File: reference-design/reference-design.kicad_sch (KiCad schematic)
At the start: 21 parts

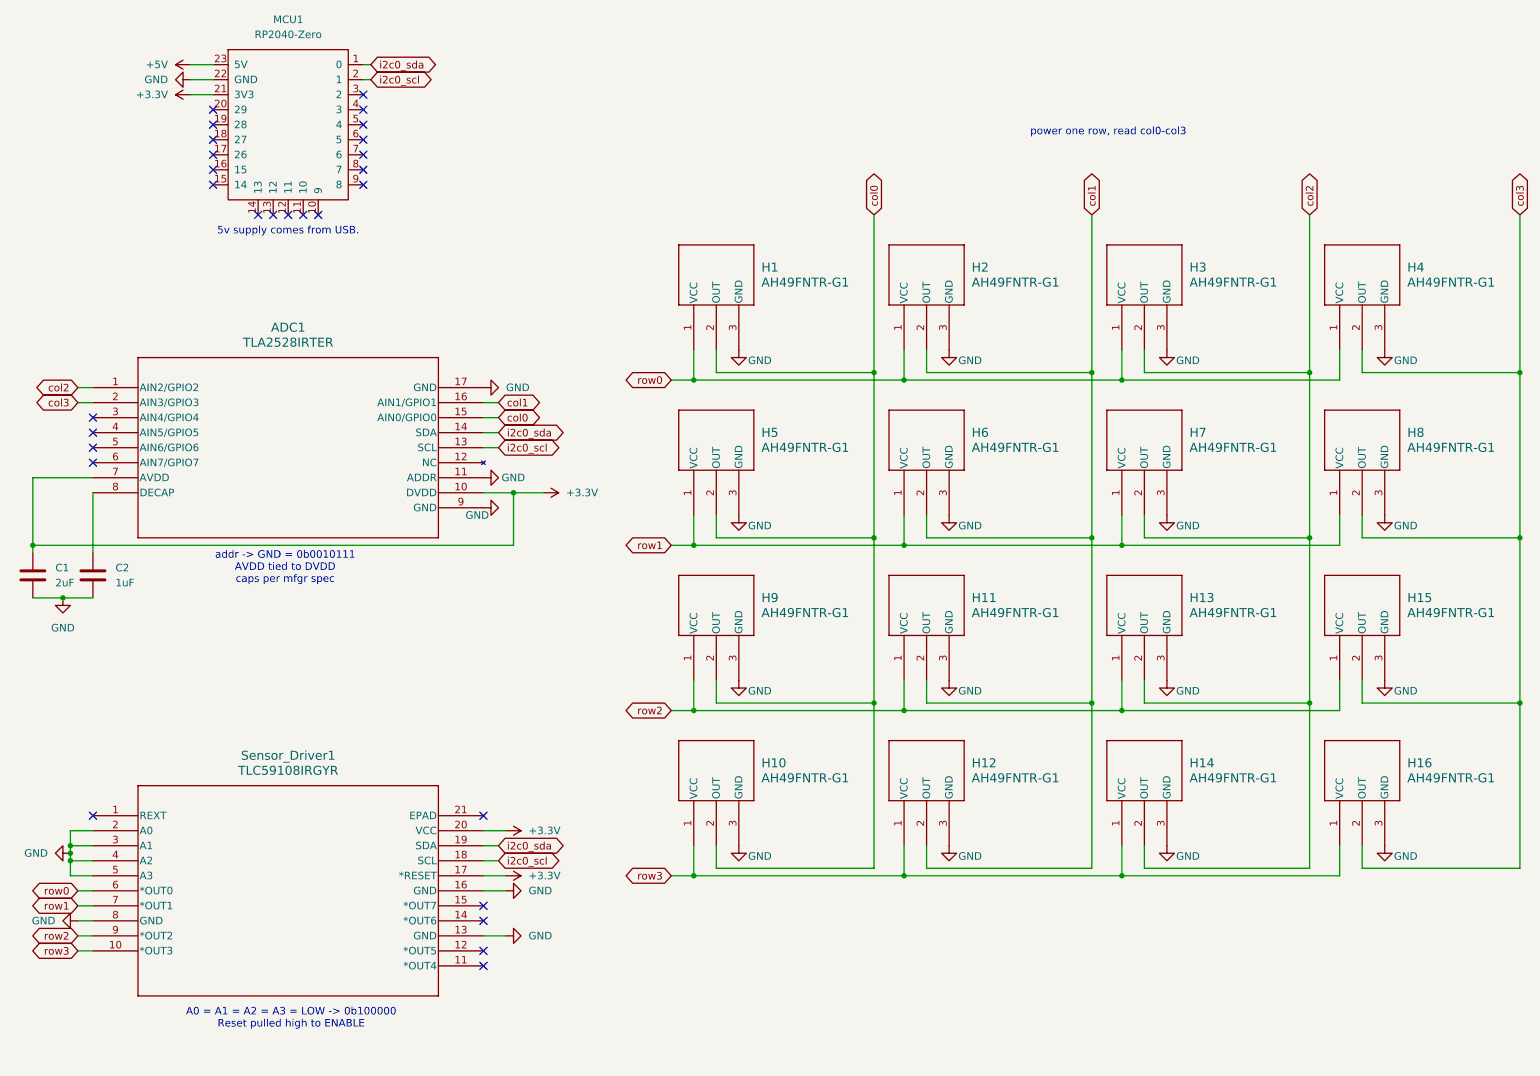
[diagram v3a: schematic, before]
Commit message: fix all but 7 warnings in ERC and DRC. notably, REXT issue still needs to be resolved
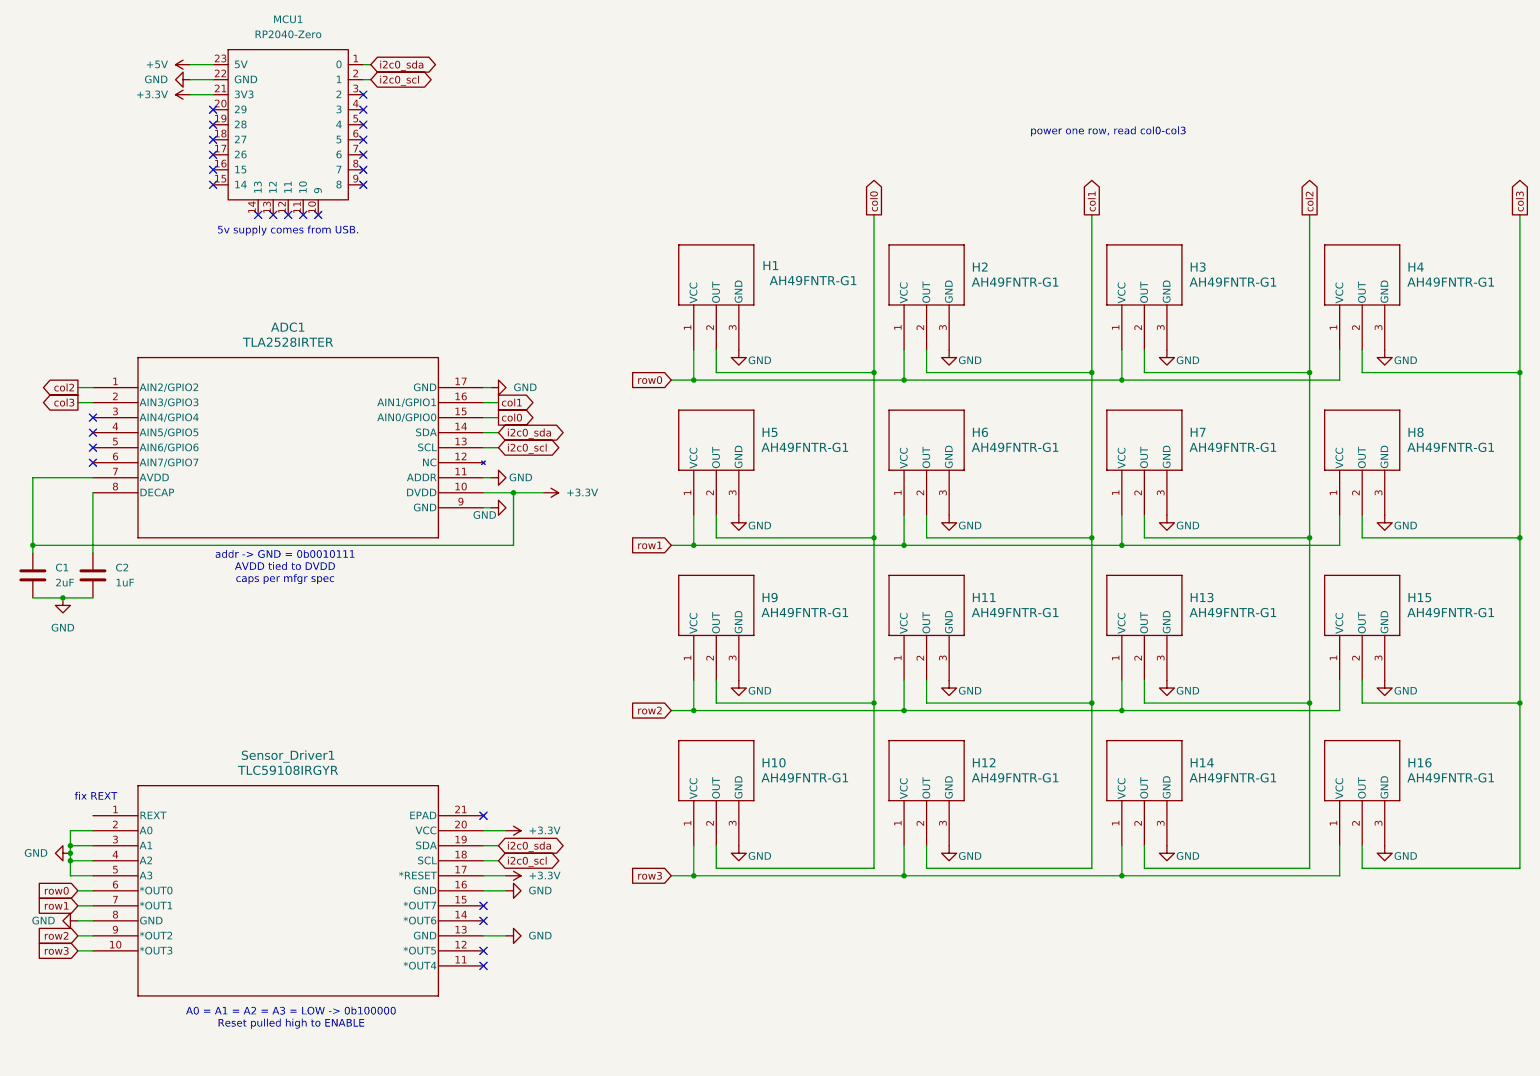
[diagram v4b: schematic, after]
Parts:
- ADC1: symbol TLA2528IRTER:TLA2528IRTER -> TLA2528IRTER_mod:TLA2528IRTER
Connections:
- no-connect marks 28 -> 27
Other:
- note added: "fix REXT"
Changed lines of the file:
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@@
 	(title_block
 		(title "ParaKeyt Reference Design")
-		(date "2025-10-21")
-		(rev "r0.1")
+		(date "2025-10-22")
+		(rev "r0.2")
 		(company "UMass ECE SDP26 Team 32")
 		(comment 1 "Bennett Gilig, Raffi Belorian, Rikhav Shah, Shlok Raval, Theo Krueger")
 	)
+	(text "fix REXT"
+		(exclude_from_sim no)
+		(at 27.178 149.352 0)
+		(effects
+			(font
+				(size 1.27 1.27)
+			)
+		)
+	)
 	(text "addr -> GND = 0b0010111\nAVDD tied to DVDD\ncaps per mfgr spec"
 		(exclude_from_sim no)
@@
 	)
 	(no_connect
-		(at 26.67 152.4)
-	)
-	(no_connect
 		(at 72.39 43.18)
 	)
@@
 	(wire
 		(pts
+			(xy 93.98 80.01) (xy 92.71 80.01)
+		)
+		(stroke
+			(width 0)
+			(type default)
+		)
+	)
+	(wire
+		(pts
 			(xy 97.79 97.79) (xy 97.79 106.68)
 		)
@@
 	(wire
 		(pts
+			(xy 93.98 100.33) (xy 92.71 100.33)
+		)
+		(stroke
+			(width 0)
+			(type default)
+		)
+	)
+	(wire
+		(pts
 			(xy 22.86 157.48) (xy 26.67 157.48)
 		)
@@
 	(wire
 		(pts
+			(xy 93.98 95.25) (xy 92.71 95.25)
+		)
+		(stroke
+			(width 0)
+			(type default)
+		)
+	)
+	(wire
+		(pts
 			(xy 200.66 162.56) (xy 237.49 162.56)
 		)
@@
 	)
 	(global_label "row3"
-		(shape bidirectional)
+		(shape input)
 		(at 24.13 175.26 180)
 		(fields_autoplaced yes)
@@
 		)
 		(property "Intersheetrefs" "${INTERSHEET_REFS}"
-			(at 15.5583 175.26 0)
+			(at 16.6696 175.26 0)
 			(effects
 				(font
@@
 	)
 	(global_label "col1"
-		(shape bidirectional)
+		(shape output)
 		(at 95.25 82.55 0)
 		(fields_autoplaced yes)
@@
 		)
 		(property "Intersheetrefs" "${INTERSHEET_REFS}"
-			(at 103.4588 82.55 0)
+			(at 102.3475 82.55 0)
 			(effects
 				(font
@@
 	)
 	(global_label "col2"
-		(shape bidirectional)
+		(shape output)
 		(at 232.41 50.8 90)
 		(fields_autoplaced yes)
@@
 		)
 		(property "Intersheetrefs" "${INTERSHEET_REFS}"
-			(at 232.41 42.5912 90)
+			(at 232.41 43.7025 90)
 			(effects
 				(font
@@
 	)
 	(global_label "row2"
-		(shape bidirectional)
+		(shape input)
 		(at 124.46 134.62 180)
 		(fields_autoplaced yes)
@@
 		)
 		(property "Intersheetrefs" "${INTERSHEET_REFS}"
-			(at 115.8883 134.62 0)
+			(at 116.9996 134.62 0)
 			(effects
 				(font
@@
 	)
 	(global_label "col0"
-		(shape bidirectional)
+		(shape output)
 		(at 158.75 50.8 90)
 		(fields_autoplaced yes)
@@
 		)
 		(property "Intersheetrefs" "${INTERSHEET_REFS}"
-			(at 158.75 42.5912 90)
+			(at 158.75 43.7025 90)
 			(effects
 				(font
@@
 	)
 	(global_label "row3"
-		(shape bidirectional)
+		(shape input)
 		(at 124.46 162.56 180)
 		(fields_autoplaced yes)
@@
 		)
 		(property "Intersheetrefs" "${INTERSHEET_REFS}"
-			(at 115.8883 162.56 0)
+			(at 116.9996 162.56 0)
 			(effects
 				(font
@@
 	)
 	(global_label "col3"
-		(shape bidirectional)
+		(shape output)
 		(at 24.13 82.55 180)
 		(fields_autoplaced yes)
@@
 		)
 		(property "Intersheetrefs" "${INTERSHEET_REFS}"
-			(at 15.9212 82.55 0)
+			(at 17.0325 82.55 0)
 			(effects
 				(font
@@
 	)
 	(global_label "row0"
-		(shape bidirectional)
+		(shape input)
 		(at 124.46 78.74 180)
 		(fields_autoplaced yes)
@@
 		)
 		(property "Intersheetrefs" "${INTERSHEET_REFS}"
-			(at 115.8883 78.74 0)
+			(at 116.9996 78.74 0)
 			(effects
 				(font
@@
 	)
 	(global_label "row1"
-		(shape bidirectional)
+		(shape input)
 		(at 24.13 167.64 180)
 		(fields_autoplaced yes)
@@
 		)
 		(property "Intersheetrefs" "${INTERSHEET_REFS}"
-			(at 15.5583 167.64 0)
+			(at 16.6696 167.64 0)
 			(effects
 				(font
@@
 	)
 	(global_label "col0"
-		(shape bidirectional)
+		(shape output)
 		(at 95.25 85.09 0)
 		(fields_autoplaced yes)
@@
 		)
 		(property "Intersheetrefs" "${INTERSHEET_REFS}"
-			(at 103.4588 85.09 0)
+			(at 102.3475 85.09 0)
 			(effects
 				(font
@@
 	)
 	(global_label "col1"
-		(shape bidirectional)
+		(shape output)
 		(at 195.58 50.8 90)
 		(fields_autoplaced yes)
@@
 		)
 		(property "Intersheetrefs" "${INTERSHEET_REFS}"
-			(at 195.58 42.5912 90)
+			(at 195.58 43.7025 90)
 			(effects
 				(font
@@
 	)
 	(global_label "row2"
-		(shape bidirectional)
+		(shape input)
 		(at 24.13 172.72 180)
 		(fields_autoplaced yes)
@@
 		)
 		(property "Intersheetrefs" "${INTERSHEET_REFS}"
-			(at 15.5583 172.72 0)
+			(at 16.6696 172.72 0)
 			(effects
 				(font
@@
 	)
 	(global_label "row0"
-		(shape bidirectional)
+		(shape input)
 		(at 24.13 165.1 180)
 		(fields_autoplaced yes)
@@
 		)
 		(property "Intersheetrefs" "${INTERSHEET_REFS}"
-			(at 15.5583 165.1 0)
+			(at 16.6696 165.1 0)
 			(effects
 				(font
@@
 	)
 	(global_label "col2"
-		(shape bidirectional)
+		(shape output)
 		(at 24.13 80.01 180)
 		(fields_autoplaced yes)
@@
 		)
 		(property "Intersheetrefs" "${INTERSHEET_REFS}"
-			(at 15.9212 80.01 0)
+			(at 17.0325 80.01 0)
 			(effects
 				(font
@@
 	)
 	(global_label "row1"
-		(shape bidirectional)
+		(shape input)
 		(at 124.46 106.68 180)
 		(fields_autoplaced yes)
@@
 		)
 		(property "Intersheetrefs" "${INTERSHEET_REFS}"
-			(at 115.8883 106.68 0)
+			(at 116.9996 106.68 0)
 			(effects
 				(font
@@
 	)
 	(global_label "col3"
-		(shape bidirectional)
+		(shape output)
 		(at 267.97 50.8 90)
 		(fields_autoplaced yes)
@@
 		)
 		(property "Intersheetrefs" "${INTERSHEET_REFS}"
-			(at 267.97 42.5912 90)
+			(at 267.97 43.7025 90)
 			(effects
 				(font
@@
 	(symbol
 		(lib_id "power:GND")
-		(at 92.71 80.01 90)
+		(at 93.98 80.01 90)
 		(unit 1)
 		(exclude_from_sim no)
@@
 		(fields_autoplaced yes)
 		(property "Reference" "#PWR024"
-			(at 99.06 80.01 0)
+			(at 100.33 80.01 0)
 			(effects
 				(font
@@
 		)
 		(property "Value" "GND"
-			(at 96.52 80.0099 90)
+			(at 97.79 80.0099 90)
 			(effects
 				(font
@@
 		)
 		(property "Footprint" ""
-			(at 92.71 80.01 0)
+			(at 93.98 80.01 0)
 			(effects
 				(font
@@
 		)
 		(property "Datasheet" ""
-			(at 92.71 80.01 0)
+			(at 93.98 80.01 0)
 			(effects
 				(font
@@
 		)
 		(property "Description" "Power symbol creates a global label with name \"GND\" , ground"
-			(at 92.71 80.01 0)
+			(at 93.98 80.01 0)
 			(effects
 				(font
@@
 	(symbol
 		(lib_id "power:GND")
-		(at 92.71 95.25 90)
+		(at 93.98 95.25 90)
 		(unit 1)
 		(exclude_from_sim no)
@@
 		(dnp no)
 		(property "Reference" "#PWR026"
-			(at 99.06 95.25 0)
+			(at 100.33 95.25 0)
 			(effects
 				(font
@@
 		)
 		(property "Value" "GND"
-			(at 95.758 95.25 90)
+			(at 97.028 95.25 90)
 			(effects
 				(font
@@
 		)
 		(property "Footprint" ""
-			(at 92.71 95.25 0)
+			(at 93.98 95.25 0)
 			(effects
 				(font
@@
 		)
 		(property "Datasheet" ""
-			(at 92.71 95.25 0)
+			(at 93.98 95.25 0)
 			(effects
 				(font
@@
 		)
 		(property "Description" "Power symbol creates a global label with name \"GND\" , ground"
-			(at 92.71 95.25 0)
+			(at 93.98 95.25 0)
 			(effects
 				(font
@@
 		(on_board yes)
 		(dnp no)
-		(fields_autoplaced yes)
 		(property "Reference" "H1"
-			(at 139.7 59.6899 90)
+			(at 142.748 59.436 90)
 			(effects
 				(font
 					(size 1.524 1.524)
 				)
-				(justify right)
+				(justify left)
 			)
 		)
 		(property "Value" "AH49FNTR-G1"
-			(at 139.7 62.2299 90)
+			(at 155.956 61.976 90)
 			(effects
 				(font
 					(size 1.524 1.524)
 				)
-				(justify right)
+				(justify left)
 			)
 		)
 		(property "Footprint" "AH49FNTR_G1:SC59_DIO"
-			(at 130.81 73.66 0)
+			(at 141.478 61.722 0)
 			(effects
 				(font
@@
 		)
 		(property "Datasheet" "AH49FNTR-G1"
-			(at 130.81 73.66 0)
+			(at 143.51 61.468 0)
 			(effects
 				(font
@@
 	(symbol
 		(lib_id "power:GND")
-		(at 92.71 100.33 90)
+		(at 93.98 100.33 90)
 		(unit 1)
 		(exclude_from_sim no)
@@
 		(dnp no)
 		(property "Reference" "#PWR02"
-			(at 99.06 100.33 0)
+			(at 100.33 100.33 0)
 			(effects
 				(font
@@
 		)
 		(property "Value" "GND"
-			(at 89.662 101.6 90)
+			(at 90.932 101.6 90)
 			(effects
 				(font
@@
 		)
 		(property "Footprint" ""
-			(at 92.71 100.33 0)
+			(at 93.98 100.33 0)
 			(effects
 				(font
@@
 		)
 		(property "Datasheet" ""
-			(at 92.71 100.33 0)
+			(at 93.98 100.33 0)
 			(effects
 				(font
@@
 		)
 		(property "Description" "Power symbol creates a global label with name \"GND\" , ground"
-			(at 92.71 100.33 0)
+			(at 93.98 100.33 0)
 			(effects
 				(font
@@
 	)
 	(symbol
-		(lib_id "TLA2528IRTER:TLA2528IRTER")
+		(lib_id "TLA2528IRTER_mod:TLA2528IRTER")
 		(at 26.67 80.01 0)
 		(unit 1)

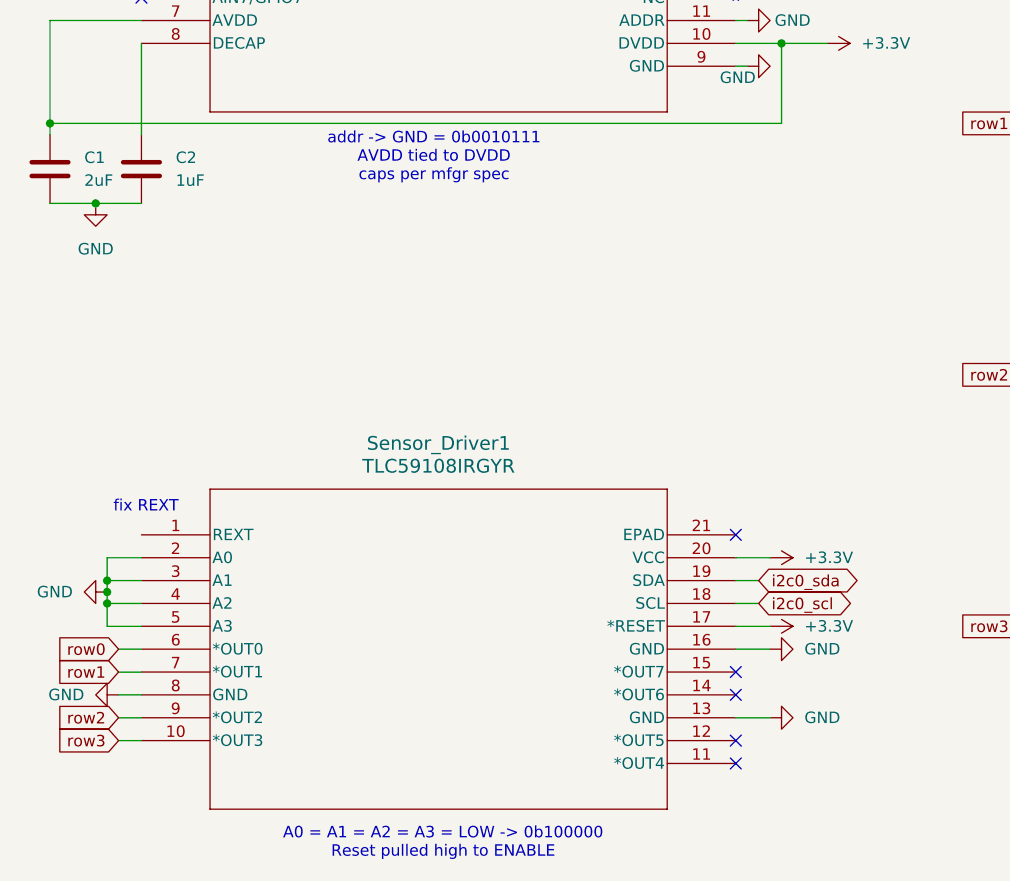
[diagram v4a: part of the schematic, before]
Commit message: swap driver for non-cc version
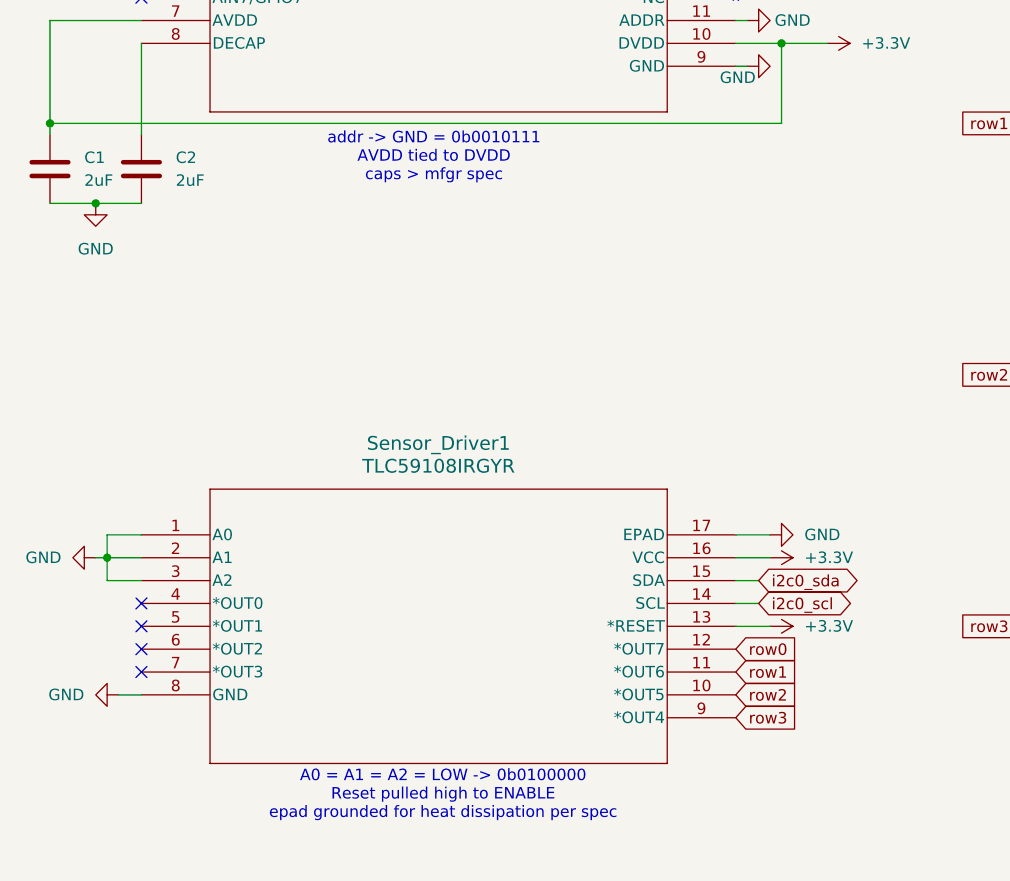
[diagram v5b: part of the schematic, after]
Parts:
- C2: value 1uF -> 2uF
- Sensor_Driver1: footprint TLC59108IRGYR:RGY20_3P05X2P05 -> RGY16_2P55X2P05; symbol TLC59108IRGYR:TLC59108IRGYR -> TLC59208FIRGYR:TLC59208FIRGYR
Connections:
- net +3.3V: now also Sensor_Driver1.13 (*RESET), Sensor_Driver1.16 (VCC); no longer Sensor_Driver1.17 (*RESET), Sensor_Driver1.20 (VCC)
- net GND: now also Sensor_Driver1.1 (A0), Sensor_Driver1.17 (EPAD); no longer Sensor_Driver1.13 (GND), Sensor_Driver1.16 (GND), Sensor_Driver1.4 (A2), Sensor_Driver1.5 (A3)
- net i2c0_scl: now also Sensor_Driver1.14 (SCL); no longer Sensor_Driver1.18 (SCL)
- net i2c0_sda: now also Sensor_Driver1.15 (SDA); no longer Sensor_Driver1.19 (SDA)
- net row0: now also Sensor_Driver1.12 (*OUT7); no longer Sensor_Driver1.6 (*OUT0)
- net row1: now also Sensor_Driver1.11 (*OUT6); no longer Sensor_Driver1.7 (*OUT1)
- net row2: now also Sensor_Driver1.10 (*OUT5); no longer Sensor_Driver1.9 (*OUT2)
- net row3: now also Sensor_Driver1.9 (*OUT4); no longer Sensor_Driver1.10 (*OUT3)
- no-connect marks 27 -> 26
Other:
- note added: "A0 = A1 = A2 = LOW -> 0b0100000 Reset pulled high to ENABLE epad grounded for heat dissipation per spec"
- note added: "addr -> GND = 0b0010111 AVDD tied to DVDD caps > mfgr spec"
- note removed: "A0 = A1 = A2 = A3 = LOW -> 0b100000 Reset pulled high to ENABLE"
- note removed: "addr -> GND = 0b0010111 AVDD tied to DVDD caps per mfgr spec"
- note removed: "fix REXT"
